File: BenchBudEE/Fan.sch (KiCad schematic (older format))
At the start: 9 parts, among them Q2 MOSFET_N, Q3 MOSFET_N, Q4 MOSFET_N, U10 MCP4922-E/P, U11 LM324

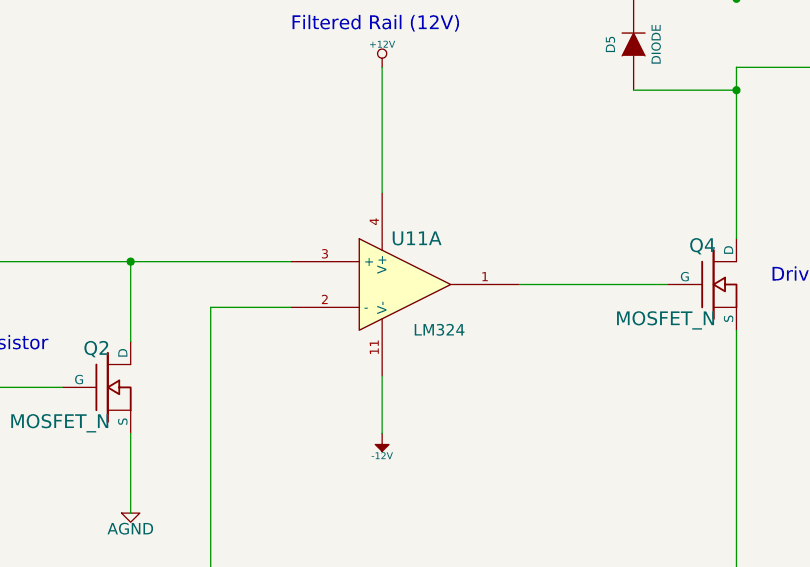
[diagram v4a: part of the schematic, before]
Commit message: Associated the Thermocouple components.
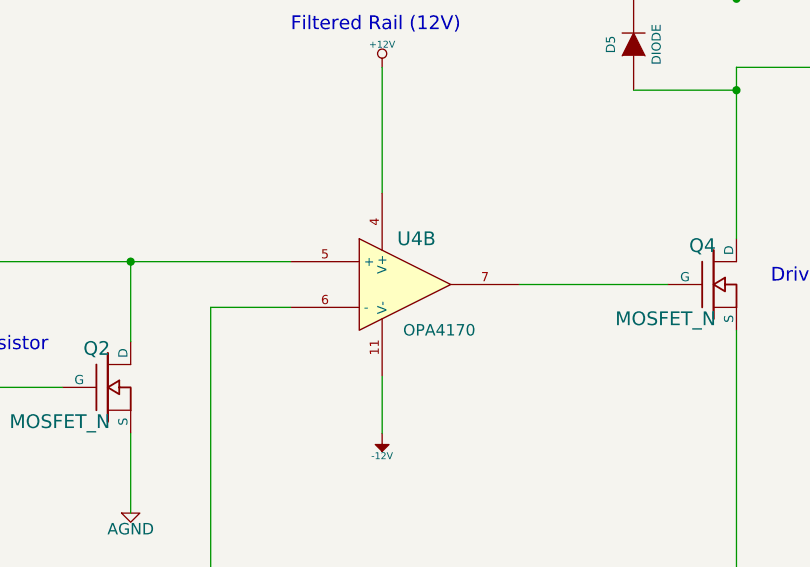
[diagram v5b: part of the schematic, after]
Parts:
- U4: renamed from U11; value LM324 -> OPA4170
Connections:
- net CURR_MEAS: now also U4.6 (-); no longer U4.2 (-)
- net at Q4.G: now also U4.7; no longer U4.1
- net at Q2.D, R24.2: now also U4.5 (+); no longer U4.3 (+)
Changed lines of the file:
@@
 Sheet 7 9
 Title ""
-Date "20 feb 2014"
+Date "21 feb 2014"
 Rev ""
 Comp ""
@@
 FAN_PWM
 $Comp
-L LM324 U11
-U 1 1 52F36291
+L LM324 U4
+U 2 1 52F36291
 P 6350 2700
-F 0 "U11" H 6400 2900 60  0000 C CNN
-F 1 "LM324" H 6500 2500 50  0000 C CNN
+F 0 "U4" H 6400 2900 60  0000 C CNN
+F 1 "OPA4170" H 6500 2500 50  0000 C CNN
 F 2 "" H 6350 2700 60  0000 C CNN
 F 3 "" H 6350 2700 60  0000 C CNN
-	1    6350 2700
+	2    6350 2700
 	1    0    0    -1
 $EndComp
@@
 $EndComp
 $Comp
-L AGND #PWR48
+L AGND #PWR048
 U 1 1 52F3630D
 P 7800 5300
-F 0 "#PWR48" H 7800 5300 40  0001 C CNN
+F 0 "#PWR048" H 7800 5300 40  0001 C CNN
 F 1 "AGND" H 7800 5230 50  0000 C CNN
 F 2 "" H 7800 5300 60  0000 C CNN
@@
 Connection ~ 7800 4050
 $Comp
-L +12V #PWR45
+L +12V #PWR049
 U 1 1 52F36343
 P 6250 1750
-F 0 "#PWR45" H 6250 1700 20  0001 C CNN
+F 0 "#PWR049" H 6250 1700 20  0001 C CNN
 F 1 "+12V" H 6250 1850 30  0000 C CNN
 F 2 "" H 6250 1750 60  0000 C CNN
@@
 	6250 1750 6250 2300
 $Comp
-L -12V #PWR46
+L -12V #PWR050
 U 1 1 52F36356
 P 6250 3350
-F 0 "#PWR46" H 6250 3480 20  0001 C CNN
+F 0 "#PWR050" H 6250 3480 20  0001 C CNN
 F 1 "-12V" H 6250 3450 30  0000 C CNN
 F 2 "" H 6250 3350 60  0000 C CNN
@@
 	4400 2600 5850 2600
 $Comp
-L AGND #PWR44
+L AGND #PWR051
 U 1 1 52F36460
 P 5150 3700
-F 0 "#PWR44" H 5150 3700 40  0001 C CNN
+F 0 "#PWR051" H 5150 3700 40  0001 C CNN
 F 1 "AGND" H 5150 3630 50  0000 C CNN
 F 2 "" H 5150 3700 60  0000 C CNN
@@
 Filtered Rail (12V)
 $Comp
-L +12C #PWR47
+L +12C #PWR052
 U 1 1 52FAE969
 P 7800 750
-F 0 "#PWR47" H 7800 720 30  0001 C CNN
+F 0 "#PWR052" H 7800 720 30  0001 C CNN
 F 1 "+12C" H 7800 860 40  0000 C CNN
 F 2 "" H 7800 750 60  0000 C CNN

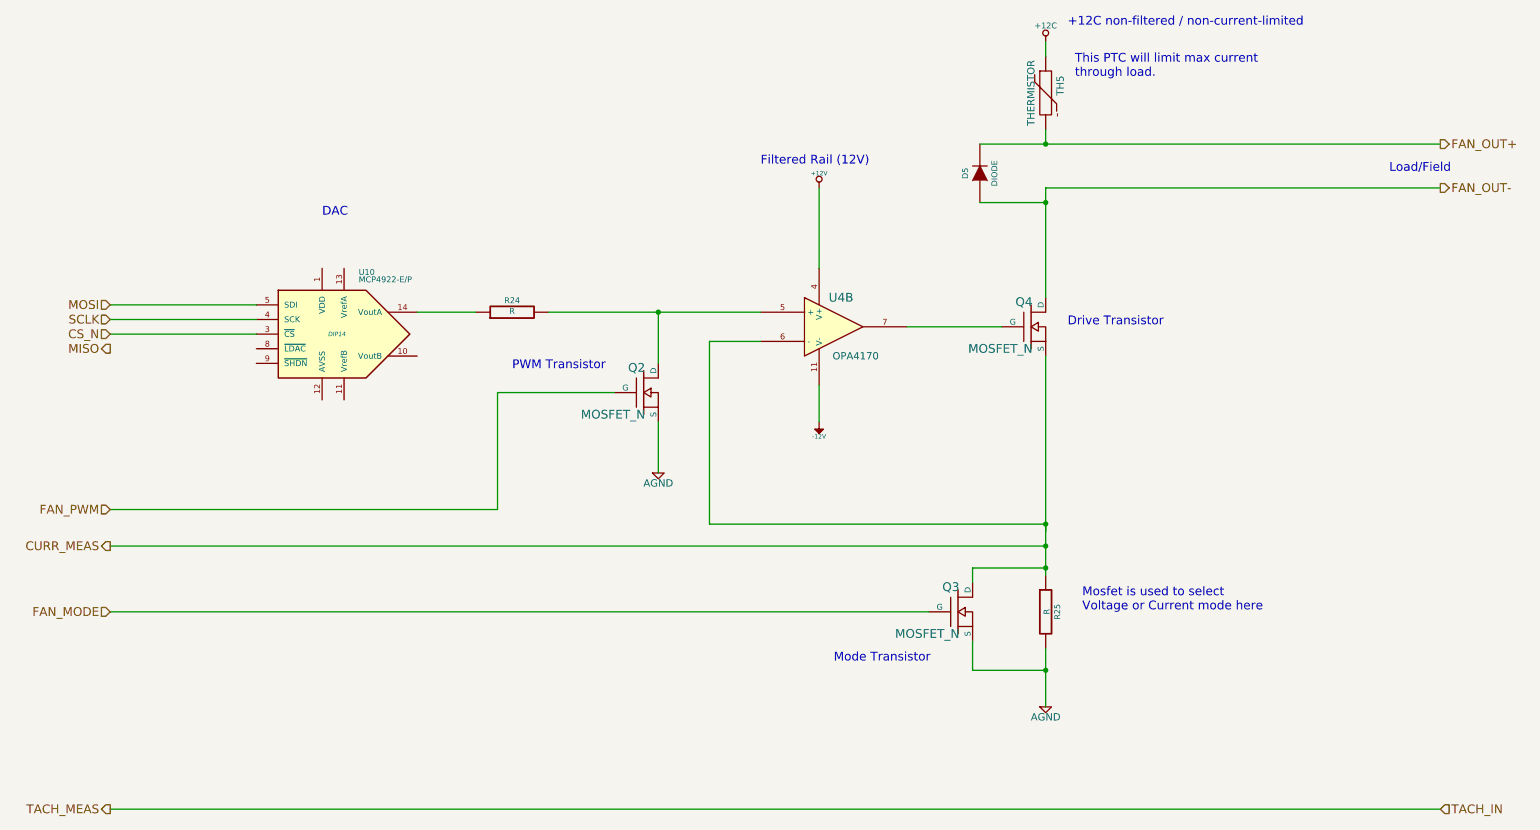
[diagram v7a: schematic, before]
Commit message: Associating the current/fan driver module components.
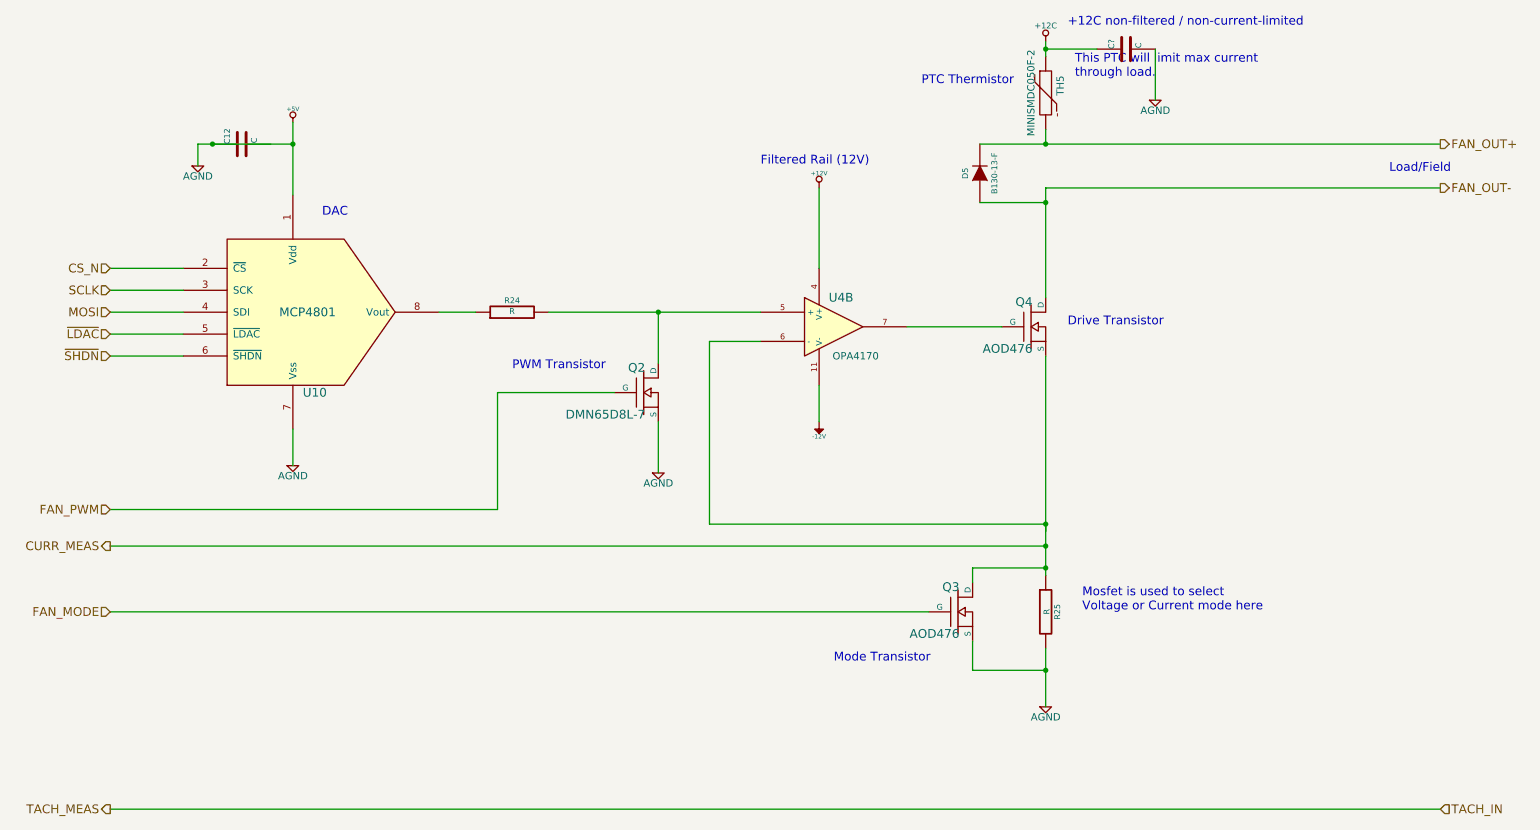
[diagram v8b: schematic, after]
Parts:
- removed U10: MCP4922-E/P, DIP14, symbol MCP4922-E/P
- added C12, C?: C, ~, symbol C
- added U10: MCP4801, symbol MCP4801
- D5: value DIODE -> B130-13-F; MFG Name (none) -> Diodes Inc; MFG Part Number (none) -> B130-13-F
- Q2: value MOSFET_N -> DMN65D8L-7; MFG Name (none) -> Diodes Inc; MFG Part Number (none) -> DMN65D8L-7
- Q3, Q4: value MOSFET_N -> AOD476; MFG Name (none) -> Alpha & Omega; MFG Part Number (none) -> AOD476
- TH5: value THERMISTOR -> MINISMDC050F-2; MFG Name (none) -> TE Connectivity; MFG Part Number (none) -> MINISMDC050F-2
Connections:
- net +12C: now also C?.1
- net CS_N: now also U10.2 (~CS)
- net MOSI: now also U10.4 (SDI)
- net SCLK: now also U10.3 (SCK)
- net at R24.1: now also U10.8 (Vout)
- net AGND renamed +5V
- net +5V: now also C12.1, C?.2, U10.1 (Vdd), U10.7 (Vss)
- new net ~LDAC: U10.5 (~LDAC)
- new net ~SHDN: U10.6 (~SHDN)
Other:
- note added: "PTC Thermistor"
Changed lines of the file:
@@
 P 7700 2700
 F 0 "Q4" H 7710 2870 60  0000 R CNN
-F 1 "MOSFET_N" H 7710 2550 60  0000 R CNN
+F 1 "AOD476" H 7710 2550 60  0000 R CNN
 F 2 "~" H 7700 2700 60  0000 C CNN
 F 3 "~" H 7700 2700 60  0000 C CNN
+F 4 "Alpha & Omega" H 7700 2700 60  0001 C CNN "MFG Name"
+F 5 "AOD476" H 7700 2700 60  0001 C CNN "MFG Part Number"
 	1    7700 2700
 	1    0    0    -1
@@
 $EndComp
 $Comp
-L AGND #PWR55
+L AGND #PWR58
 U 1 1 52F3630D
 P 7800 5300
-F 0 "#PWR55" H 7800 5300 40  0001 C CNN
+F 0 "#PWR58" H 7800 5300 40  0001 C CNN
 F 1 "AGND" H 7800 5230 50  0000 C CNN
 F 2 "" H 7800 5300 60  0000 C CNN
@@
 Connection ~ 7800 4050
 $Comp
-L +12V #PWR52
+L +12V #PWR55
 U 1 1 52F36343
 P 6250 1750
-F 0 "#PWR52" H 6250 1700 20  0001 C CNN
+F 0 "#PWR55" H 6250 1700 20  0001 C CNN
 F 1 "+12V" H 6250 1850 30  0000 C CNN
 F 2 "" H 6250 1750 60  0000 C CNN
@@
 	6250 1750 6250 2300
 $Comp
-L -12V #PWR53
+L -12V #PWR56
 U 1 1 52F36356
 P 6250 3350
-F 0 "#PWR53" H 6250 3480 20  0001 C CNN
+F 0 "#PWR56" H 6250 3480 20  0001 C CNN
 F 1 "-12V" H 6250 3450 30  0000 C CNN
 F 2 "" H 6250 3350 60  0000 C CNN
@@
 	4400 2600 5850 2600
 $Comp
-L AGND #PWR51
+L AGND #PWR54
 U 1 1 52F36460
 P 5150 3700
-F 0 "#PWR51" H 5150 3700 40  0001 C CNN
+F 0 "#PWR54" H 5150 3700 40  0001 C CNN
 F 1 "AGND" H 5150 3630 50  0000 C CNN
 F 2 "" H 5150 3700 60  0000 C CNN
 F 3 "" H 5150 3700 60  0000 C CNN
 	1    5150 3700
-	1    0    0    -1
-$EndComp
-$Comp
-L MCP4922-E/P U10
-U 1 1 52F36479
-P 2950 2750
-F 0 "U10" H 3100 3150 40  0000 L BNN
-F 1 "MCP4922-E/P" H 3100 3100 40  0000 L BNN
-F 2 "DIP14" H 2950 2750 30  0000 C CIN
-F 3 "" H 2950 2750 60  0000 C CNN
-	1    2950 2750
 	1    0    0    -1
 $EndComp
@@
 	0    -1   -1   0
 $EndComp
-Wire Wire Line
-	3900 2600 3500 2600
-Text HLabel 1400 2550 0    60   Input ~ 0
+Text HLabel 1400 2600 0    60   Input ~ 0
 MOSI
-Text HLabel 1400 2850 0    60   Output ~ 0
-MISO
-Text HLabel 1400 2750 0    60   Input ~ 0
+Text HLabel 1400 2300 0    60   Input ~ 0
 CS_N
-Text HLabel 1400 2650 0    60   Input ~ 0
+Text HLabel 1400 2450 0    60   Input ~ 0
 SCLK
-Wire Wire Line
-	1400 2550 2400 2550
-Wire Wire Line
-	1400 2650 2400 2650
-Wire Wire Line
-	1400 2750 2400 2750
 Text Notes 2850 1950 0    60   ~ 0
 DAC
@@
 P 7200 4650
 F 0 "Q3" H 7210 4820 60  0000 R CNN
-F 1 "MOSFET_N" H 7210 4500 60  0000 R CNN
+F 1 "AOD476" H 7210 4500 60  0000 R CNN
 F 2 "~" H 7200 4650 60  0000 C CNN
 F 3 "~" H 7200 4650 60  0000 C CNN
+F 4 "Alpha & Omega" H 7200 4650 60  0001 C CNN "MFG Name"
+F 5 "AOD476" H 7200 4650 60  0001 C CNN "MFG Part Number"
 	1    7200 4650
 	1    0    0    -1
@@
 P 7800 1100
 F 0 "TH5" V 7900 1150 50  0000 C CNN
-F 1 "THERMISTOR" V 7700 1100 50  0000 C CNN
+F 1 "MINISMDC050F-2" V 7700 1100 50  0000 C CNN
 F 2 "~" H 7800 1100 60  0000 C CNN
 F 3 "~" H 7800 1100 60  0000 C CNN
+F 4 "TE Connectivity" H 7800 1100 60  0001 C CNN "MFG Name"
+F 5 "MINISMDC050F-2" H 7800 1100 60  0001 C CNN "MFG Part Number"
 	1    7800 1100
 	1    0    0    -1
@@
 P 7350 1650
 F 0 "D5" H 7350 1750 40  0000 C CNN
-F 1 "DIODE" H 7350 1550 40  0000 C CNN
+F 1 "B130-13-F" H 7350 1550 40  0000 C CNN
 F 2 "~" H 7350 1650 60  0000 C CNN
 F 3 "~" H 7350 1650 60  0000 C CNN
+F 4 "Diodes Inc" H 7350 1650 60  0001 C CNN "MFG Name"
+F 5 "B130-13-F" H 7350 1650 60  0001 C CNN "MFG Part Number"
 	1    7350 1650
 	0    -1   -1   0
@@
 P 5050 3150
 F 0 "Q2" H 5060 3320 60  0000 R CNN
-F 1 "MOSFET_N" H 5060 3000 60  0000 R CNN
+F 1 "DMN65D8L-7" H 5060 3000 60  0000 R CNN
 F 2 "~" H 5050 3150 60  0000 C CNN
 F 3 "~" H 5050 3150 60  0000 C CNN
+F 4 "Diodes Inc" H 5050 3150 60  0001 C CNN "MFG Name"
+F 5 "DMN65D8L-7" H 5050 3150 60  0001 C CNN "MFG Part Number"
 	1    5050 3150
 	1    0    0    -1
@@
 Filtered Rail (12V)
 $Comp
-L +12C #PWR54
+L +12C #PWR57
 U 1 1 52FAE969
 P 7800 750
-F 0 "#PWR54" H 7800 720 30  0001 C CNN
+F 0 "#PWR57" H 7800 720 30  0001 C CNN
 F 1 "+12C" H 7800 860 40  0000 C CNN
 F 2 "" H 7800 750 60  0000 C CNN
@@
 Text Notes 6350 5000 0    60   ~ 0
 Mode Transistor
+$Comp
+L MCP4801 U10
+U 1 1 53089F82
+P 2650 2600
+F 0 "U10" H 2800 2050 60  0000 C CNN
+F 1 "MCP4801" H 2750 2600 60  0000 C CNN
+F 2 "" H 2550 2650 60  0000 C CNN
+F 3 "" H 2550 2650 60  0000 C CNN
+	1    2650 2600
+	1    0    0    -1
+$EndComp
+Wire Wire Line
+	3650 2600 3900 2600
+Wire Wire Line
+	1400 2300 1900 2300
+Wire Wire Line
+	1400 2450 1900 2450
+Wire Wire Line
+	1400 2600 1900 2600
+Text HLabel 1400 2750 0    60   Input ~ 0
+~LDAC
+Wire Wire Line
+	1400 2750 1900 2750
+Text HLabel 1400 2900 0    60   Input ~ 0
+~SHDN
+Wire Wire Line
+	1400 2900 1900 2900
+$Comp
+L C C12
+U 1 1 53090CF4
+P 2300 1450
+F 0 "C12" H 2300 1550 40  0000 L CNN
+F 1 "C" H 2306 1365 40  0000 L CNN
+F 2 "~" H 2338 1300 30  0000 C CNN
+F 3 "~" H 2300 1450 60  0000 C CNN
+	1    2300 1450
+	0    -1   -1   0
+$EndComp
+Wire Wire Line
+	2000 1450 2650 1450
+Wire Wire Line
+	2650 1300 2650 1800
+Connection ~ 2650 1450
+$Comp
+L AGND #PWR51
+U 1 1 53090CFD
+P 2000 1600
+F 0 "#PWR51" H 2000 1600 40  0001 C CNN
+F 1 "AGND" H 2000 1530 50  0000 C CNN
+F 2 "" H 2000 1600 60  0000 C CNN
+F 3 "" H 2000 1600 60  0000 C CNN
+	1    2000 1600
+	1    0    0    -1
+$EndComp
+Wire Wire Line
+	2000 1600 2000 1450
+Connection ~ 2100 1450
+$Comp
+L +5V #PWR52
+U 1 1 53090D05
+P 2650 1300
+F 0 "#PWR52" H 2650 1390 20  0001 C CNN
+F 1 "+5V" H 2650 1390 30  0000 C CNN
+F 2 "" H 2650 1300 60  0000 C CNN
+F 3 "" H 2650 1300 60  0000 C CNN
+	1    2650 1300
+	1    0    0    -1
+$EndComp
+$Comp
+L AGND #PWR53
+U 1 1 53090D0B
+P 2650 3650
+F 0 "#PWR53" H 2650 3650 40  0001 C CNN
+F 1 "AGND" H 2650 3580 50  0000 C CNN
+F 2 "" H 2650 3650 60  0000 C CNN
+F 3 "" H 2650 3650 60  0000 C CNN
+	1    2650 3650
+	1    0    0    -1
+$EndComp
+Wire Wire Line
+	2650 3400 2650 3650
+Text Notes 6950 1050 0    60   ~ 0
+PTC Thermistor
+$Comp
+L C C?
+U 1 1 5308A319
+P 8350 800
+F 0 "C?" H 8350 900 40  0000 L CNN
+F 1 "C" H 8356 715 40  0000 L CNN
+F 2 "~" H 8388 650 30  0000 C CNN
+F 3 "~" H 8350 800 60  0000 C CNN
+	1    8350 800
+	0    -1   -1   0
+$EndComp
+Wire Wire Line
+	8150 800  7800 800
+Connection ~ 7800 800
+$Comp
+L AGND #PWR?
+U 1 1 5308A34F
+P 8550 1150
+F 0 "#PWR?" H 8550 1150 40  0001 C CNN
+F 1 "AGND" H 8550 1080 50  0000 C CNN
+F 2 "" H 8550 1150 60  0000 C CNN
+F 3 "" H 8550 1150 60  0000 C CNN
+	1    8550 1150
+	1    0    0    -1
+$EndComp
+Wire Wire Line
+	8550 1150 8550 800
 $EndSCHEMATC
